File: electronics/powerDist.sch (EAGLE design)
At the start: 54 parts, among them CON1 B3B-ZR, IC1 TPS6300, IC2 TPS77033, J1 2MMPAD, J2 2MMPAD, J3 2MMPAD, J4 2MMPAD, J5 2MMPAD, J6 2MMPAD, J7 2MMPAD, J8 2MMPAD, J9 2MMPAD, U1 DRV8830, U2 MSP430F5500IRGZR, U3 DRV8830, U4 DRV8830

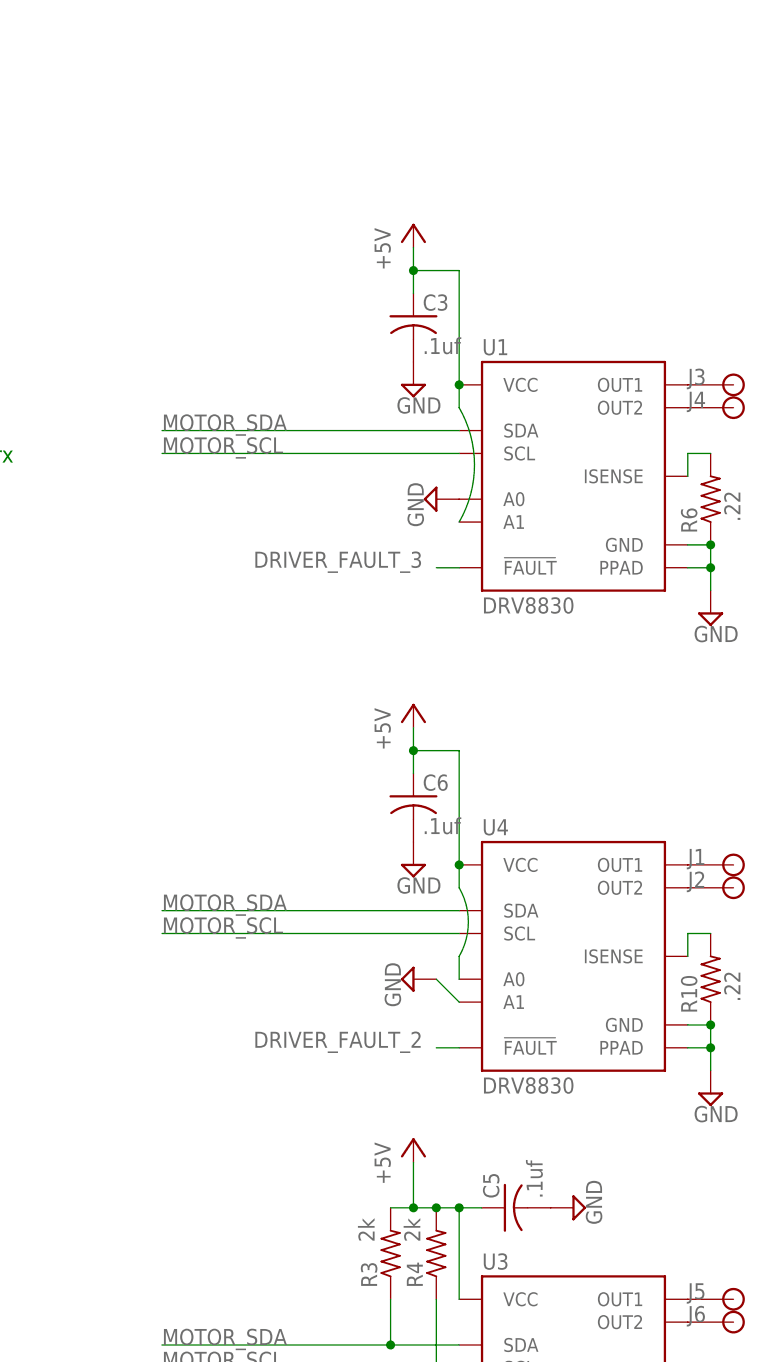
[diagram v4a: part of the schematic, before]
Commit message: added single chip imu, need to hooking up.  Investigate i2c compatablity
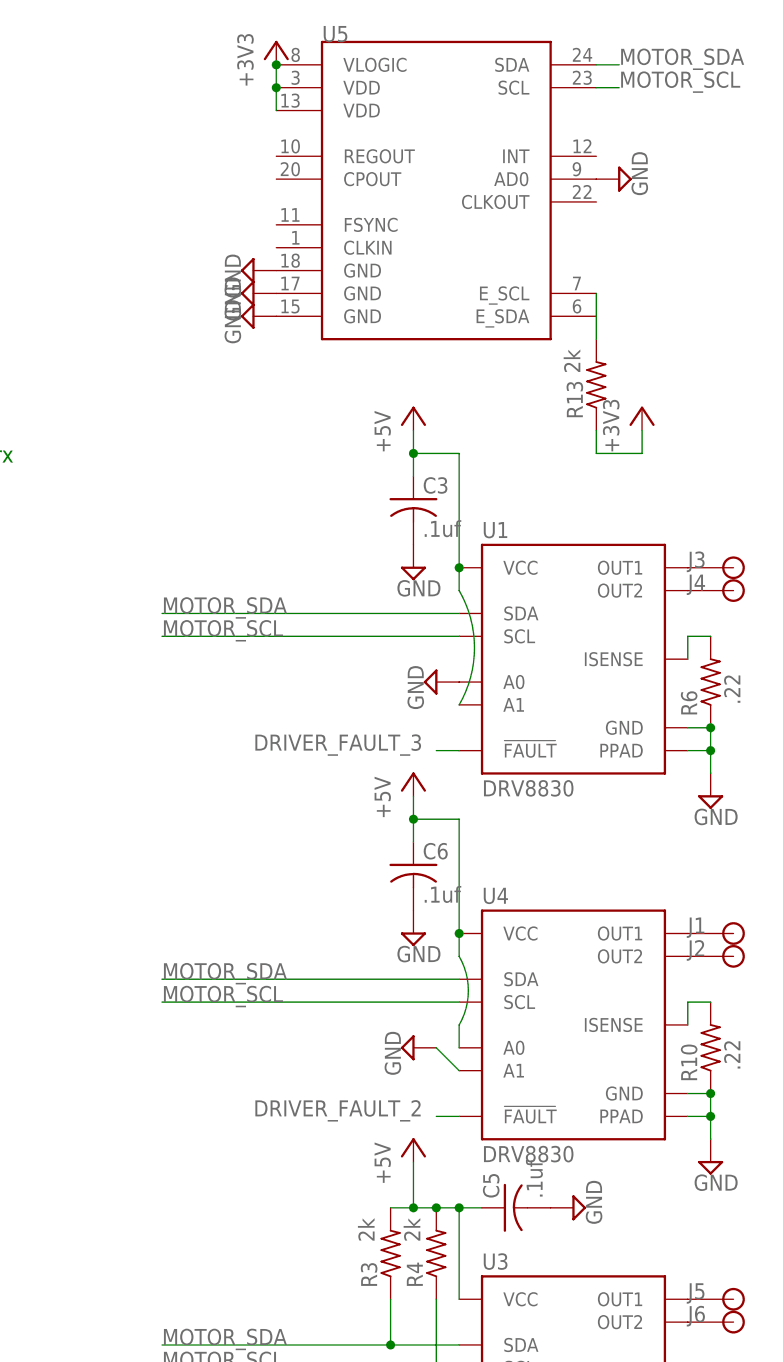
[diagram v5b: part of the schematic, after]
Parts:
- added R13: 2k, rcl:R-US_R0402
- added U5: (no value), SparkFun-Sensors:MPU-9150QFN-24-NP
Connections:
- new net N$21: R13.2, U5.E_SCL, U5.E_SDA
- net +3V3: now also R13.1, U5.VDD@13, U5.VDD@3, U5.VLOGIC
- net GND: now also U5.AD0, U5.GND@15, U5.GND@17, U5.GND@18
- net MOTOR_SCL: now also U5.SCL
- net MOTOR_SDA: now also U5.SDA
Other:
- moved on the sheet: C3, C6, J1, J2, J3, J4, R10, R6, U1, U4

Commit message: worked on imu layout/sch.
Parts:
- added C23, C24, C25: .1uf, rcl:C-USC0603
- C1, C2: value (none) -> 10F
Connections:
- net MOTOR_SCL renamed SYS_SCL
- net MOTOR_SDA renamed SYS_SDA
- new net IMU_INT: U2.P1.3/TA0.2, U5.INT
- new net N$22: C24.1, U5.REGOUT
- new net N$23: C25.1, U5.CPOUT
- net +3V3: now also C23.1
- net DRIVER_FAULT_1: now also U2.P1.0/TA0CLK/ACLK
- net DRIVER_FAULT_2: now also U2.P1.1/TA0.0
- net DRIVER_FAULT_3: now also U2.P1.2/TA0.1
- net GND: now also C23.2, C24.2, C25.2, U5.CLKIN, U5.FSYNC
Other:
- moved on the sheet: C10, C11, C12, C13, C14, C15, C16, C17, C20, C21, C22, R1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

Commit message: continuing work on layout
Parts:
- added J10: 2MMPAD, connectors:2MMPAD
- C8: value 10uf -> .1uf
- renumbered U$1 to Q1
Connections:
- net GND: now also J10.P$1
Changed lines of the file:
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@@
 <part name="R9" library="rcl" deviceset="R-US_" device="R0402" value="200k"/>
 <part name="SUPPLY17" library="supply2" deviceset="GND" device=""/>
-<part name="C8" library="rcl" deviceset="C-US" device="C0603" value="10uf"/>
+<part name="C8" library="rcl" deviceset="C-US" device="C0603" value=".1uf"/>
 <part name="C9" library="rcl" deviceset="C-US" device="C0603" value="10uf"/>
 <part name="SUPPLY18" library="supply2" deviceset="GND" device=""/>
@@
 <part name="J8" library="connectors" deviceset="2MMPAD" device=""/>
 <part name="J9" library="connectors" deviceset="2MMPAD" device=""/>
-<part name="U$1" library="SparkFun-FreqCtrl" deviceset="CRYSTAL-GROUNDED" device="" value="25Mhz"/>
+<part name="Q1" library="SparkFun-FreqCtrl" deviceset="CRYSTAL-GROUNDED" device="" value="25Mhz"/>
 <part name="SUPPLY38" library="supply2" deviceset="GND" device=""/>
 <part name="C20" library="rcl" deviceset="C-US" device="C0603" value="18pf"/>
@@
 <part name="SUPPLY42" library="supply2" deviceset="GND" device=""/>
 <part name="SUPPLY43" library="supply2" deviceset="GND" device=""/>
+<part name="J10" library="connectors" deviceset="2MMPAD" device=""/>
 </parts>
 <sheets>
@@
 <attribute name="NAME" x="-10.16" y="109.22" size="1.778" layer="95" rot="R180"/>
 </instance>
-<instance part="U$1" gate="G$1" x="152.4" y="-5.08" smashed="yes" rot="R90">
+<instance part="Q1" gate="G$1" x="152.4" y="-5.08" smashed="yes" rot="R90">
 <attribute name="VALUE" x="149.86" y="-7.62" size="1.778" layer="96" rot="R90"/>
 </instance>
@@
 <instance part="SUPPLY42" gate="GND" x="177.8" y="106.68"/>
 <instance part="SUPPLY43" gate="GND" x="185.42" y="104.14"/>
+<instance part="J10" gate="G$1" x="-15.24" y="104.14" smashed="yes" rot="R180">
+<attribute name="NAME" x="-10.16" y="104.14" size="1.778" layer="95" rot="R180"/>
+</instance>
 </instances>
 <busses>
@@
 <junction x="38.1" y="109.22"/>
 <pinref part="J9" gate="G$1" pin="P$1"/>
+<pinref part="J10" gate="G$1" pin="P$1"/>
+<wire x1="-10.16" y1="104.14" x2="-10.16" y2="109.22" width="0.1524" layer="91"/>
+<junction x="-10.16" y="109.22"/>
 </segment>
 <segment>
@@
 </segment>
 <segment>
-<pinref part="U$1" gate="G$1" pin="3"/>
+<pinref part="Q1" gate="G$1" pin="3"/>
 <pinref part="SUPPLY38" gate="GND" pin="GND"/>
 </segment>
@@
 </segment>
 <segment>
+<wire x1="20.32" y1="-5.08" x2="20.32" y2="-15.24" width="0.1524" layer="91"/>
+<wire x1="20.32" y1="-15.24" x2="7.62" y2="-30.48" width="0.1524" layer="91"/>
+<label x="-12.7" y="-30.48" size="1.778" layer="95"/>
 <pinref part="U2" gate="A" pin="P1.0/TA0CLK/ACLK"/>
-<wire x1="30.48" y1="-5.08" x2="27.94" y2="-5.08" width="0.1524" layer="91"/>
-<label x="7.62" y="-5.08" size="1.778" layer="95"/>
+<wire x1="30.48" y1="-5.08" x2="20.32" y2="-5.08" width="0.1524" layer="91"/>
 </segment>
 </net>
@@
 </segment>
 <segment>
+<wire x1="22.86" y1="-7.62" x2="22.86" y2="-15.24" width="0.1524" layer="91"/>
+<wire x1="22.86" y1="-15.24" x2="7.62" y2="-33.02" width="0.1524" layer="91"/>
+<label x="-12.7" y="-33.02" size="1.778" layer="95"/>
 <pinref part="U2" gate="A" pin="P1.1/TA0.0"/>
-<wire x1="30.48" y1="-7.62" x2="27.94" y2="-7.62" width="0.1524" layer="91"/>
-<label x="7.62" y="-7.62" size="1.778" layer="95"/>
+<wire x1="30.48" y1="-7.62" x2="22.86" y2="-7.62" width="0.1524" layer="91"/>
 </segment>
 </net>
@@
 </segment>
 <segment>
+<wire x1="25.4" y1="-10.16" x2="25.4" y2="-17.78" width="0.1524" layer="91"/>
+<wire x1="25.4" y1="-17.78" x2="7.62" y2="-35.56" width="0.1524" layer="91"/>
+<label x="-12.7" y="-35.56" size="1.778" layer="95"/>
 <pinref part="U2" gate="A" pin="P1.2/TA0.1"/>
-<wire x1="30.48" y1="-10.16" x2="27.94" y2="-10.16" width="0.1524" layer="91"/>
-<label x="7.62" y="-10.16" size="1.778" layer="95"/>
+<wire x1="25.4" y1="-10.16" x2="30.48" y2="-10.16" width="0.1524" layer="91"/>
 </segment>
 </net>
@@
 <wire x1="116.84" y1="-5.08" x2="147.32" y2="-5.08" width="0.1524" layer="91"/>
 <wire x1="147.32" y1="-5.08" x2="147.32" y2="0" width="0.1524" layer="91"/>
-<pinref part="U$1" gate="G$1" pin="2"/>
+<pinref part="Q1" gate="G$1" pin="2"/>
 <wire x1="147.32" y1="0" x2="152.4" y2="0" width="0.1524" layer="91"/>
 <pinref part="C20" gate="G$1" pin="1"/>
@@
 <segment>
 <pinref part="U2" gate="A" pin="P5.3/XT2OUT"/>
-<pinref part="U$1" gate="G$1" pin="1"/>
+<pinref part="Q1" gate="G$1" pin="1"/>
 <wire x1="116.84" y1="-7.62" x2="152.4" y2="-7.62" width="0.1524" layer="91"/>
 <pinref part="C21" gate="G$1" pin="1"/>
@@
 </segment>
 <segment>
+<wire x1="27.94" y1="-12.7" x2="27.94" y2="-17.78" width="0.1524" layer="91"/>
+<wire x1="27.94" y1="-17.78" x2="7.62" y2="-38.1" width="0.1524" layer="91"/>
+<label x="-12.7" y="-38.1" size="1.778" layer="95"/>
 <pinref part="U2" gate="A" pin="P1.3/TA0.2"/>
-<wire x1="30.48" y1="-12.7" x2="27.94" y2="-12.7" width="0.1524" layer="91"/>
-<label x="7.62" y="-12.7" size="1.778" layer="95"/>
-</segment>
-</net>
+<wire x1="27.94" y1="-12.7" x2="30.48" y2="-12.7" width="0.1524" layer="91"/>
+</segment>
+</net>
